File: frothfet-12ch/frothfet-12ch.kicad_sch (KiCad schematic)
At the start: 8 parts

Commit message: schematic looking clean.
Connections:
- net ADC0_SS is gone; now on net ADC1_CS: U1.16 (GPIO10)
- net ADC1_CS: no longer U1.11 (GPIO18)
- new net ADC2_CS: U1.11 (GPIO18)
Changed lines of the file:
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@@
 		)
 	)
-	(global_label "ADC0_CS"
+	(global_label "ADC1_CS"
 		(shape input)
 		(at 270.51 36.83 0)
@@
 		)
 	)
-	(global_label "ADC0_SS"
+	(global_label "ADC1_CS"
 		(shape input)
 		(at 116.84 97.79 180)
@@
 		)
 		(property "Intersheetrefs" "${INTERSHEET_REFS}"
-			(at 105.6301 97.79 0)
+			(at 105.5696 97.79 0)
 			(effects
 				(font
@@
 		)
 	)
-	(global_label "ADC1_CS"
+	(global_label "ADC2_CS"
 		(shape input)
 		(at 270.51 107.95 0)
@@
 		)
 	)
-	(global_label "ADC1_CS"
+	(global_label "ADC2_CS"
 		(shape input)
 		(at 116.84 85.09 180)

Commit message: updated bom
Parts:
- R1, R2: LCSC (none) -> C114561
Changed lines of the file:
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@@
+			)
+		)
+		(property "LCSC" "C114561"
+			(at 77.47 80.01 0)
+			(effects
+				(font
+					(size 1.27 1.27)
+				)
+				(hide yes)
 			)
 		)
@@
 			(at 87.63 80.01 0)
 			(effects
+				(font
+					(size 1.27 1.27)
+				)
+				(hide yes)
+			)
+		)
+		(property "LCSC" "C114561"
+			(at 87.63 80.01 0)
+			(effects

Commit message: just need to route it...
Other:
- company: https://github.com/hoeken/yarrboard -> https://github.com/hoeken/frothfet
- title: Yarrboard 8ch Mosfet Driver -> FrothFET 12CH
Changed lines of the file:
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@@
 	(paper "A4")
 	(title_block
-		(title "Yarrboard 8ch Mosfet Driver")
-		(rev "C1")
-		(company "https://github.com/hoeken/yarrboard")
+		(title "FrothFET 12CH")
+		(date "2024-08-17")
+		(rev "D")
+		(company "https://github.com/hoeken/frothfet")
 	)
 	(junction

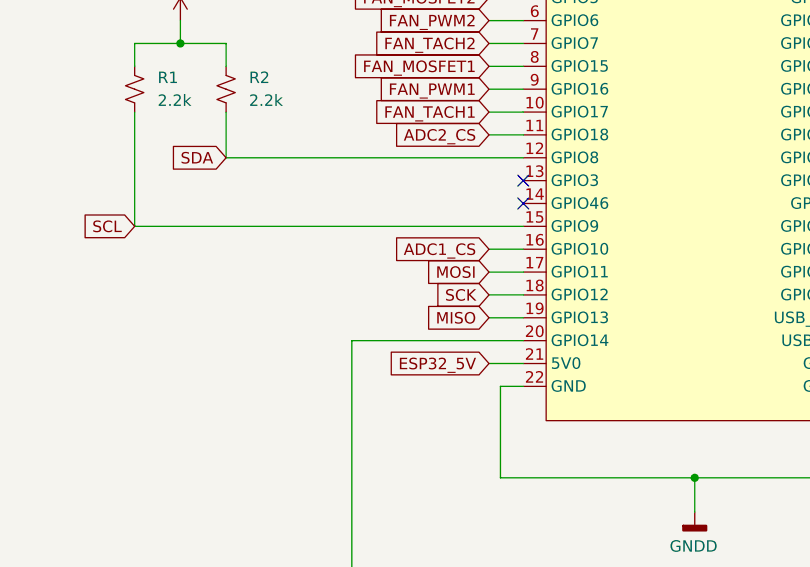
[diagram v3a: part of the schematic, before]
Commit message: fully routed
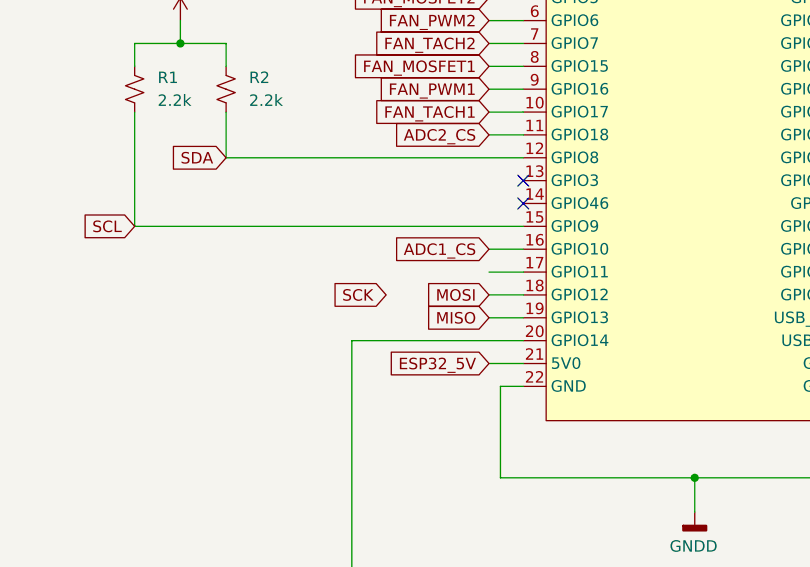
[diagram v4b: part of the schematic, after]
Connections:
- net MOSI: now also U1.18 (GPIO12); no longer U1.17 (GPIO11)
- net SCK: no longer U1.18 (GPIO12)
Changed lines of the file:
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@@
 	(global_label "MOSI"
 		(shape input)
-		(at 116.84 100.33 180)
+		(at 116.84 102.87 180)
 		(fields_autoplaced yes)
 		(effects
@@
 		)
 		(property "Intersheetrefs" "${INTERSHEET_REFS}"
-			(at 109.2586 100.33 0)
+			(at 109.2586 102.87 0)
 			(effects
 				(font
@@
 	(global_label "SCK"
 		(shape input)
-		(at 116.84 102.87 180)
+		(at 105.41 102.87 180)
 		(fields_autoplaced yes)
 		(effects
@@
 		)
 		(property "Intersheetrefs" "${INTERSHEET_REFS}"
-			(at 110.1053 102.87 0)
+			(at 98.6753 102.87 0)
 			(effects
 				(font

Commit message: clean drc
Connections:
- net SCK: now also U1.17 (GPIO11)
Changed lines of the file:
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@@
 	(global_label "SCK"
 		(shape input)
-		(at 105.41 102.87 180)
+		(at 116.84 100.33 180)
 		(fields_autoplaced yes)
 		(effects
@@
 		)
 		(property "Intersheetrefs" "${INTERSHEET_REFS}"
-			(at 98.6753 102.87 0)
+			(at 110.1053 100.33 0)
 			(effects
 				(font

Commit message: erc clean
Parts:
- U1: footprint yarrboard:Waveshare-ESP32-S3-dev-kit -> (none)
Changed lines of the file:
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@@
+	(wire
+		(pts
+			(xy 110.49 59.69) (xy 116.84 59.69)
+		)
+		(stroke
+			(width 0)
+			(type default)
+		)
+	)
 	(wire
 		(pts
@@
 			)
 		)
-		(property "Footprint" "yarrboard:Waveshare-ESP32-S3-dev-kit"
+		(property "Footprint" ""
 			(at 139.7 54.61 0)
 			(effects
@@
 			)
 		)
-		(property "Description" ""
+		(property "Description" "Power symbol creates a global label with name \"GNDA\" , analog ground"
 			(at 54.61 67.31 0)
 			(effects
@@
 			)
 		)
-		(property "Description" ""
+		(property "Description" "Power symbol creates a global label with name \"GNDD\" , digital ground"
 			(at 139.7 127 0)
 			(effects
@@
 			)
 		)
-		(property "Description" ""
+		(property "Description" "Power symbol creates a global label with name \"+3.3V\""
 			(at 82.55 72.39 0)
 			(effects
@@
 			)
 		)
-		(property "Description" ""
+		(property "Description" "Power symbol creates a global label with name \"+3.3V\""
 			(at 53.34 38.1 0)
 			(effects
@@
 	)
 	(symbol
+		(lib_id "power:PWR_FLAG")
+		(at 110.49 59.69 0)
+		(unit 1)
+		(exclude_from_sim no)
+		(in_bom yes)
+		(on_board yes)
+		(dnp no)
+		(fields_autoplaced yes)
+		(property "Reference" "#FLG010"
+			(at 110.49 57.785 0)
+			(effects
+				(font
+					(size 1.27 1.27)
+				)
+				(hide yes)
+			)
+		)
+		(property "Value" "PWR_FLAG"
+			(at 110.49 54.61 0)
+			(effects
+				(font
+					(size 1.27 1.27)
+				)
+			)
+		)
+		(property "Footprint" ""
+			(at 110.49 59.69 0)
+			(effects
+				(font
+					(size 1.27 1.27)
+				)
+				(hide yes)
+			)
+		)
+		(property "Datasheet" "~"
+			(at 110.49 59.69 0)
+			(effects
+				(font
+					(size 1.27 1.27)
+				)
+				(hide yes)
+			)
+		)
+		(property "Description" "Special symbol for telling ERC where power comes from"
+			(at 110.49 59.69 0)
+			(effects
+				(font
+					(size 1.27 1.27)
+				)
+				(hide yes)
+			)
+		)
+		(pin "1"
+		)
+		(instances
+			(project "frothfet-12ch"
+				(path "/c83c6236-96e9-46ad-9d7a-9e2efa4a7966"
+					(reference "#FLG010")
+					(unit 1)
+				)
+			)
+		)
+	)
+	(symbol
 		(lib_id "power:+3.3V")
 		(at 116.84 55.88 0)
@@
 			)
 		)
-		(property "Description" ""
+		(property "Description" "Power symbol creates a global label with name \"+3.3V\""
 			(at 116.84 55.88 0)
 			(effects
@@
 			)
 		)
-		(property "Description" ""
+		(property "Description" "Power symbol creates a global label with name \"GNDD\" , digital ground"
 			(at 31.75 191.77 0)
 			(effects
@@
 			)
 		)
-		(property "Description" ""
+		(property "Description" "Power symbol creates a global label with name \"GNDD\" , digital ground"
 			(at 166.37 60.96 0)
 			(effects

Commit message: more pre-production tweaks
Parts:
- U1: footprint (none) -> yarrboard:Waveshare-ESP32-S3-dev-kit
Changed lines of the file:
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@@
 			)
 		)
-		(property "Footprint" ""
+		(property "Footprint" "yarrboard:Waveshare-ESP32-S3-dev-kit"
 			(at 139.7 54.61 0)
 			(effects

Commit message: lots of big updates
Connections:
- net ADC3_CS: now reaches U1.13 (GPIO3)
- net CHANNEL 10/PWM: no longer names the net of U1.28 (GPIO47)
- net CHANNEL 11/PWM: no longer names the net of U1.27 (GPIO21)
- net CHANNEL 12/PWM: no longer names the net of U1.20 (GPIO14)
- net CHANNEL 9/PWM: no longer names the net of U1.29 (GPIO48)
- no-connect marks 12 -> 11
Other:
- sheet CURRENT ADC1 renamed HIRES ADC1
- removed sheet CHANNEL 10
- removed sheet CHANNEL 11
- removed sheet CHANNEL 12
- removed sheet CHANNEL 9
- removed sheet CURRENT ADC2
- removed sheet INPUT 1
- removed sheet INPUT 2
- removed sheet INPUT 3
- removed sheet INPUT 4
- removed sheet VOLTAGE ADC3
- moved on the sheet: R1, R2, U1
